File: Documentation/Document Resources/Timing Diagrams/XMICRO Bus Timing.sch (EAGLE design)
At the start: 0 parts

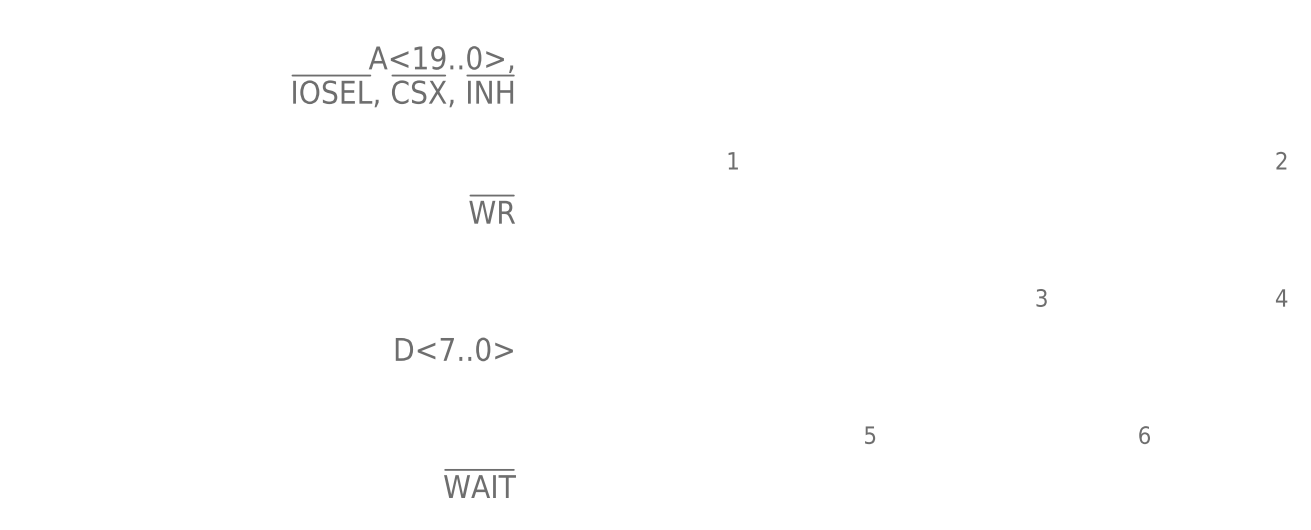
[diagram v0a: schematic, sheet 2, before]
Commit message: Updated timing specs, changed physical drawings font
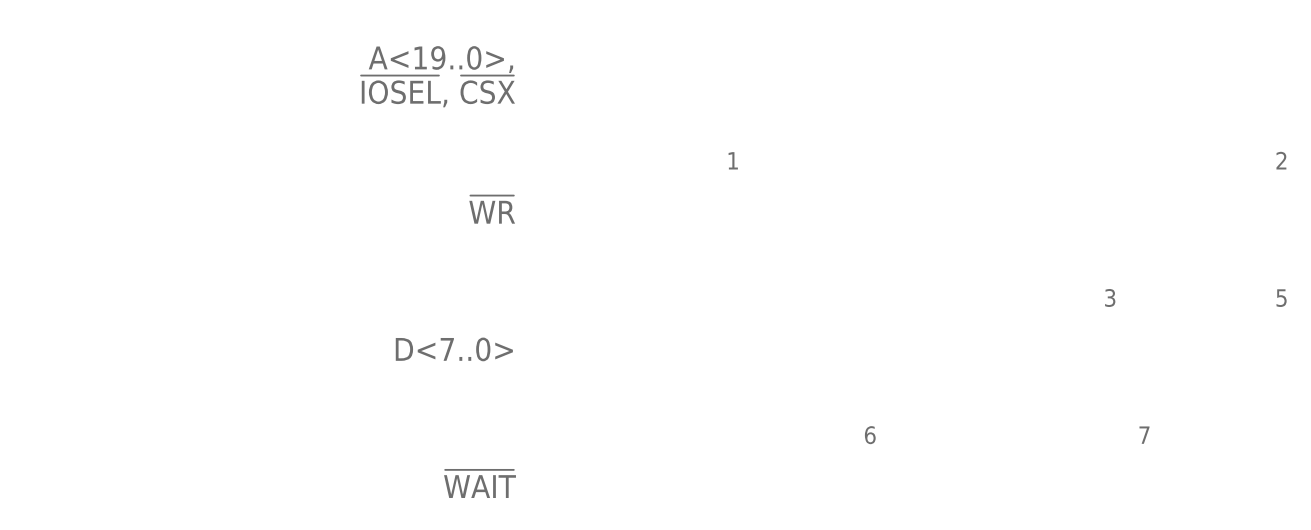
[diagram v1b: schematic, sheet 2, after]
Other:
- note added: "7"
- note added: "A<19..0>, !IOSEL!, !CSX!"
- note removed: "A<19..0>, !IOSEL!, !CSX!, !INH!"

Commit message: Updated specification
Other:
- note added: "A<19..0>, !IOSEL!, !CSX!, !INH!"
- note removed: "A<19..0>, !IOSEL!, !CSX!"
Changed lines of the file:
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@@
 <setting verticaltext="up"/>
 </settings>
-<grid distance="0.1" unitdist="inch" unit="inch" style="lines" multiple="1" display="no" altdistance="0.05" altunitdist="inch" altunit="inch"/>
+<grid distance="0.1" unitdist="inch" unit="inch" style="lines" multiple="1" display="no" altdistance="0.01" altunitdist="inch" altunit="inch"/>
 <layers>
 <layer number="91" name="Nets" color="2" fill="1" visible="yes" active="yes"/>
@@
 <plain>
 <text x="-5.08" y="-2.54" size="2.54" layer="95" align="center-right">A&lt;19..0&gt;,
-!IOSEL!, !CSX!</text>
+!IOSEL!, !CSX!,
+!INH!</text>
 <text x="-5.08" y="-17.78" size="2.54" layer="95" align="center-right">!RD!</text>
 <text x="-5.08" y="-33.02" size="2.54" layer="95" align="center-right">D&lt;7..0&gt;</text>
@@
 <plain>
 <text x="-5.08" y="-2.54" size="2.54" layer="95" align="center-right">A&lt;19..0&gt;,
-!IOSEL!, !CSX!</text>
+!IOSEL!, !CSX!,
+!INH!</text>
 <text x="-5.08" y="-17.78" size="2.54" layer="95" align="center-right">!WR!</text>
 <text x="-5.08" y="-33.02" size="2.54" layer="95" align="center-right">D&lt;7..0&gt;</text>
